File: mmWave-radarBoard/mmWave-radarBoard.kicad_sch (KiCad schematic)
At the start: 6 parts, among them J101 Conn_01x03_Socket, J102 Conn_01x07_Socket

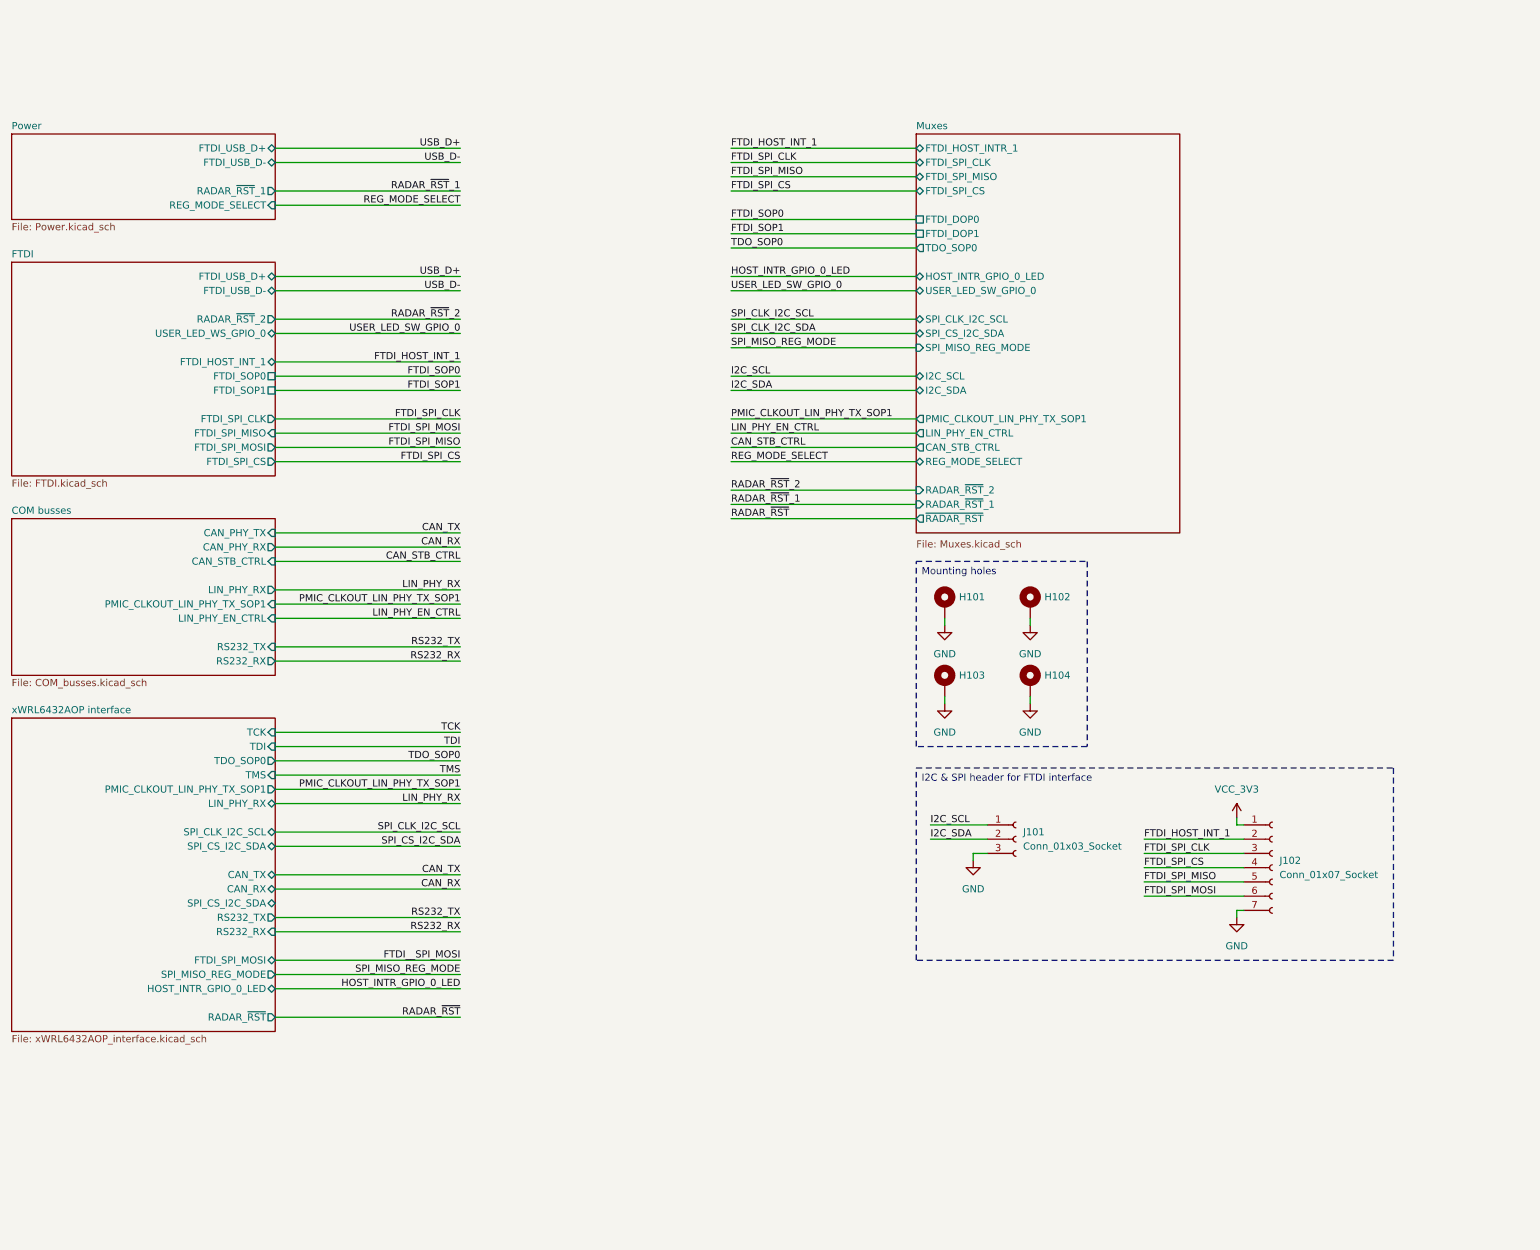
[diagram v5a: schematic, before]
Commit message: Updated schematic and PCB
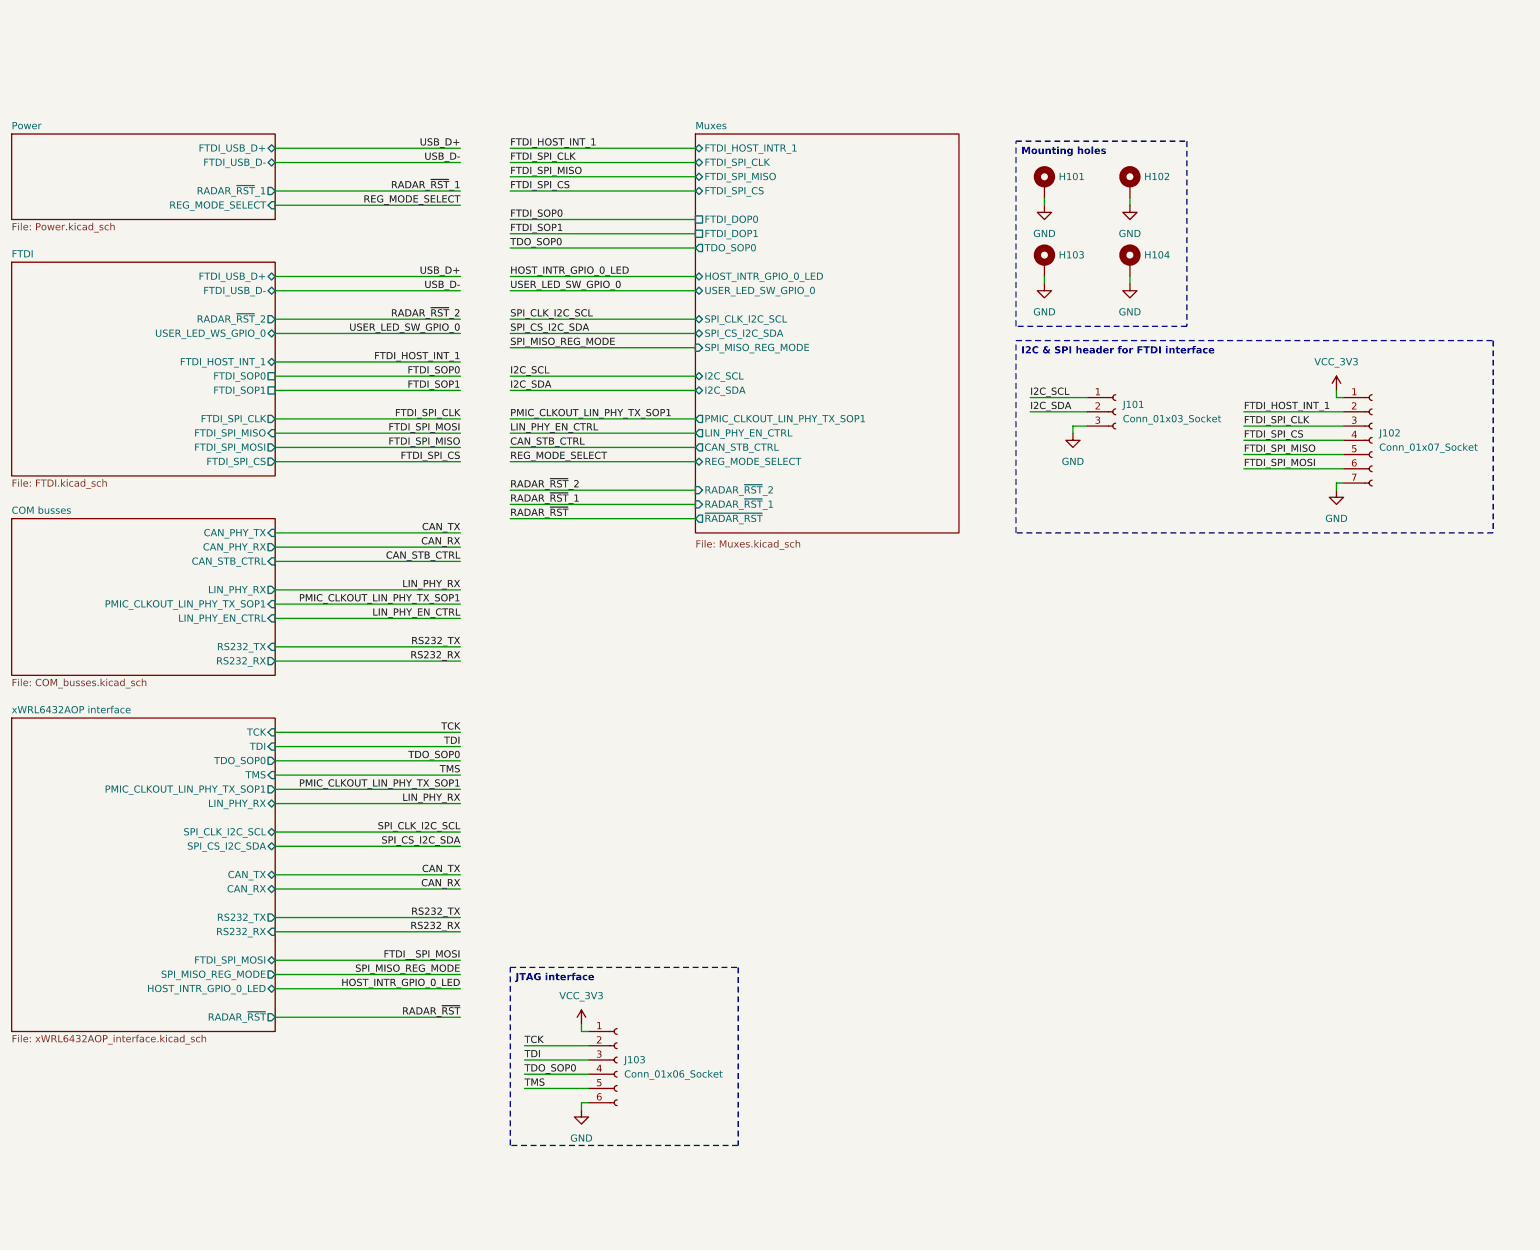
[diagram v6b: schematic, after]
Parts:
- added J103: Conn_01x06_Socket, symbol Connector:Conn_01x06_Socket
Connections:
- net GND: now also J103.6 (Pin_6)
- net TCK: now also J103.2 (Pin_2)
- net TDI: now also J103.3 (Pin_3)
- net TDO_SOP0: now also J103.4 (Pin_4)
- net TMS: now also J103.5 (Pin_5)
- net VCC_3V3: now also J103.1 (Pin_1)
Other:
- moved on the sheet: H101, H102, H103, H104, J101, J102

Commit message: Updated PCB and schematic
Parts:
- J103: footprint (none) -> Connector_JST:JST_ZH_B6B-ZR_1x06_P1.50mm_Vertical
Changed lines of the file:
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@@
 			"AAAAAAAAAAAAAAAAAAAAAAAAAAAAAAAAAAAAAAAAAAAAAAAAAAAAAAAAAAAAAAAAAAAAAAAAAAAA"
 			"AAAAAAAAAAAAAAAAAAAAAAAAAAAAAAAAAAAAAAAAAAAAAAAAAAAAAAAAAAAAAAAAAAAAAAAAAAAA"
-			"AAAAAAAAAAAAAAAAAAAAAAAAAAAAAAAAAAAAAAAAAAAAAAAAAAAAAAAAAAAAAA=="
+			"AAAAAAAAAAAAAAAAAAAAAAAAAAAAAAAAAAAAAAAAAAAAAAAAAAAAAAAAAAAAAABjAGIAagAvAGcA"
+			"ZQBzAGMANgA4AHIAdABlAGQATQBGAFkAagAxAHAAMwBVAEMAeQBJAGwANABsAHIAZQArAHYAegBn"
+			"AEEAOABIADMAdwBYAGUAYgAxAEIAbwBCAEMANwAyAEwAbwA2AFcANwBZAG4AZABIAFMAVwBXAGsA"
+			"WgBkAGMAYgBDADUAZQArAGkATgBtAC8AbgB1AFUARQBuAFYAeQB3ADUAKwAwADQAQQBBAEUAcQBQ"
+			"AG4AdwB5AFoANABtAGIAQwBjAGUANQBiAHYAdgBlAFgAMQA2ADAAawA4ACsATQBCAHgARgBUAGMA"
+			"TAB4AHkAdQBQAHgAcAA5AHIAUgBPADgAQwBRADMATQBFAGcAUQBLAEEAQQBpAGIAagBsAFUARABW"
+			"AHQAZgBlAGUAWQB6AFIAcwBIADMASABuAGwAQQBwAEEARABsAG4AcgB2ADMAbgBiAEQAKwA0ADkA"
+			"dABZAGYASgBkADgAQgBCAEEAQQBnAG8AdwArAEwAeABQAGYAYQBLAHUAWAA2ADkAYQB0ADYAKwBK"
+			"AGEASABBAHAAQwBWADkANABrAEgAcABKAHYAdwAyADIAUgBRAGgAYgB0ADIARgArAHMAOQBTAEcA"
+			"ZgBVAGwAUABFAG0AZwAzAHYAegBOAHgAZwB4AEcAQwBHAEUAZgBpAGUAWgBwAFQAZQBUAGwAcABM"
+			"AGwAUgByAEsATgBhAGYAbwBuAHkAcQBvADcAcAAxAFcAMQBmAEgAdwBZAFAAbgBIAGwAMgBWAHUA"
+			"VQBaADIAOQBoAFYANgBIAFIATQAxAEIARgBCAHMANgB3AEMANQAxAGgAMQArAGkAZQBrAHQAWgBK"
+			"AFoAZABaAE4AYgAyAEcAOQBnAC8ASgBMAHMARABsAGQASQAzAGoAbABkAEYAYQA0ADYASwB4AG8A"
+			"KwBoAG0AcgBSAEEAZABhAEwARAA5AGgAcwBiAHoAeABtAGkAMgA3AFEAUAAwAFQAeQBVAGsAbgBt"
+			"AHIAMQAzAGoAUwBiADgATABUAEcASgBUAEQAdQBXAFYATgBaAGcAYgBiAE0AdgBwAHgAawA3ADgA"
+			"awA4AEoATABaAHQAUwBhADcAbgBsADIAZgA4AEkASQBZAFEAUQBRAHUAagAzAHcASgBBADgAUQBn"
+			"AGcAaABoAEIAQgBDAGIAWQBoAGYAZABaAFcARAA0AGQAVwBkAHoAQQBIAEcAUgB5ADgAMwBaAHoA"
+			"MgB0AGUATABYAHEARQBQAHUAMwAxAE4AZABmAEsASAAyADYATQA0AEMAMwBNAEQARQB1AFUAdwBD"
+			"AG8AUQBPACsAaQBPAHIAUgBYAFYAYgAyADkAeQB3AGEAUAAwAFcARwBFAFgANg=="
 		)
 	)
@@
 			)
 		)
-		(property "Footprint" ""
+		(property "Footprint" "Connector_JST:JST_ZH_B6B-ZR_1x06_P1.50mm_Vertical"
 			(at 123.19 181.61 0)
 			(effects
